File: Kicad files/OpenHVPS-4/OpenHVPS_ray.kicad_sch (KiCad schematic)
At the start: 70 parts, among them J1 Conn_01x03_Male, J2 Conn_01x03_Male, Q1 FQT7N10, Q2 BC846A, Q3 MMDT3906, U1 MAX6008AEUR+T, U2 74HC14, U3 MAX4162, U4 CD14538BM

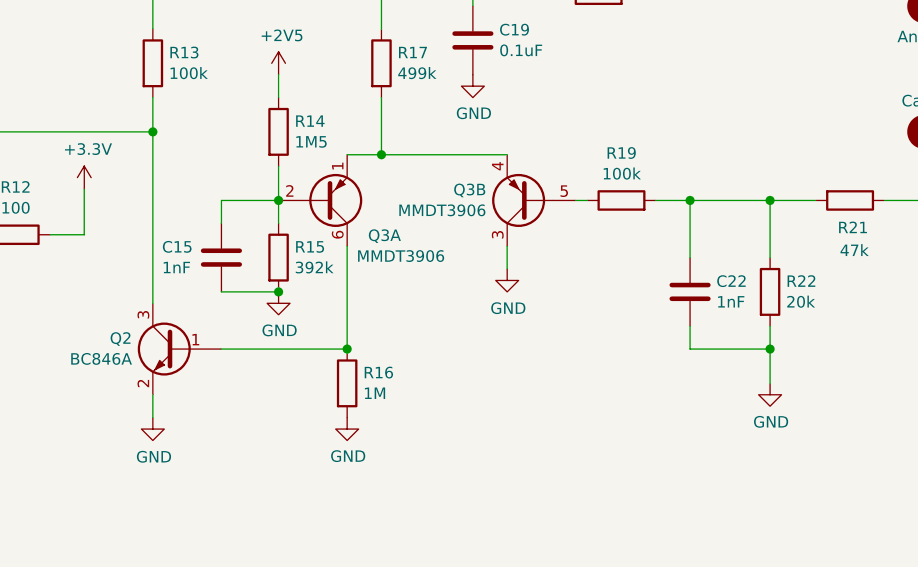
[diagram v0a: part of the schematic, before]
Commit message: Corrected C22 value to 360pF updated BOM
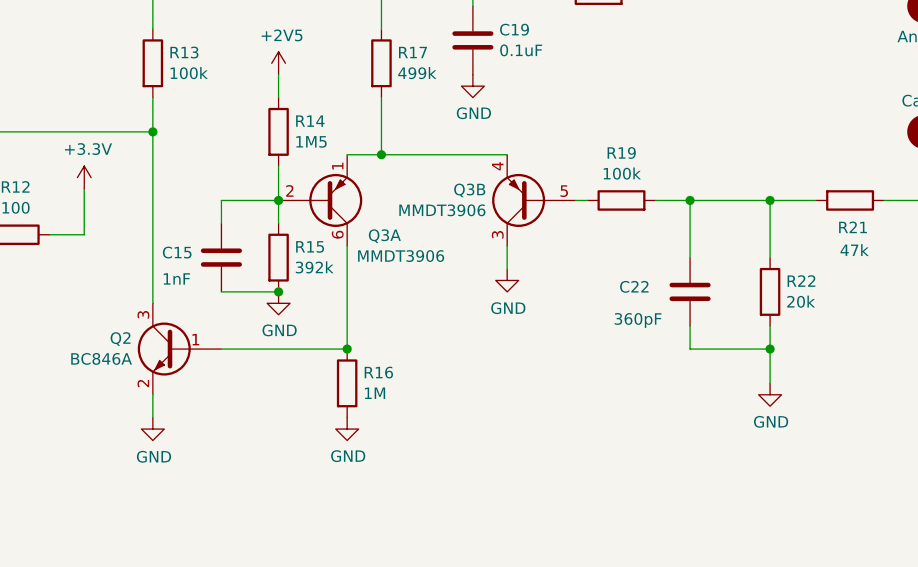
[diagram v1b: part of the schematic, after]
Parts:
- C22: value 1nF -> 360pF
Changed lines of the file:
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@@
       (effects (font (size 1.27 1.27)) hide)
     )
-    (property "Datasheet" "https://www.digikey.com/en/products/detail/tdk-corporation/C1005X7R1H102K050BA/513719" (id 3) (at 101.6 164.465 0)
+    (property "Datasheet" "https://www.digikey.com/en/products/detail/tdk-corporation/C2012C0G2A102J060AA/789714" (id 3) (at 101.6 164.465 0)
       (effects (font (size 1.27 1.27)) hide)
     )
@@
   (symbol (lib_id "Device:C") (at 200.66 140.335 0) (unit 1)
     (in_bom yes) (on_board yes)
-    (property "Reference" "C15" (id 0) (at 194.0561 139.1856 0)
-      (effects (font (size 1.27 1.27)) (justify left))
-    )
-    (property "Value" "1nF" (id 1) (at 194.056 141.484 0)
+    (property "Reference" "C15" (id 0) (at 194.0561 139.8206 0)
+      (effects (font (size 1.27 1.27)) (justify left))
+    )
+    (property "Value" "1nF" (id 1) (at 194.056 142.754 0)
       (effects (font (size 1.27 1.27)) (justify left))
     )
@@
       (effects (font (size 1.27 1.27)) hide)
     )
-    (property "Datasheet" "https://www.digikey.com/en/products/detail/tdk-corporation/C1005X7R1H102K050BA/513719" (id 3) (at 200.66 140.335 0)
+    (property "Datasheet" "https://www.digikey.com/en/products/detail/tdk-corporation/C2012C0G2A102J060AA/789714" (id 3) (at 200.66 140.335 0)
       (effects (font (size 1.27 1.27)) hide)
     )
@@
   (symbol (lib_id "Device:C") (at 252.73 144.145 0) (unit 1)
     (in_bom yes) (on_board yes)
-    (property "Reference" "C22" (id 0) (at 255.6511 142.9956 0)
-      (effects (font (size 1.27 1.27)) (justify left))
-    )
-    (property "Value" "1nF" (id 1) (at 255.651 145.294 0)
+    (property "Reference" "C22" (id 0) (at 244.8561 143.6306 0)
+      (effects (font (size 1.27 1.27)) (justify left))
+    )
+    (property "Value" "360pF" (id 1) (at 244.221 147.199 0)
       (effects (font (size 1.27 1.27)) (justify left))
     )
@@
       (effects (font (size 1.27 1.27)) hide)
     )
-    (property "Datasheet" "https://www.digikey.com/en/products/detail/tdk-corporation/C1005X7R1H102K050BA/513719" (id 3) (at 252.73 144.145 0)
+    (property "Datasheet" "https://www.digikey.com/en/products/detail/kemet/C0805C361J1GAC7800/2212653" (id 3) (at 252.73 144.145 0)
       (effects (font (size 1.27 1.27)) hide)
     )
@@
     )
     (path "/743b7e51-503f-44bc-a063-83e91538f340"
-      (reference "C22") (unit 1) (value "1nF") (footprint "Capacitor_SMD:C_0805_2012Metric")
+      (reference "C22") (unit 1) (value "360pF") (footprint "Capacitor_SMD:C_0805_2012Metric")
     )
     (path "/00000000-0000-0000-0000-0000600ddc6a"
